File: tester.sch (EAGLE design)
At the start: 74 parts, among them IC1 ATmega8/88/168, K1 NA 05W K, M1 SP6000C-180, P1 250, P2 10k lin, Q1 BC847CSMD, Q2 BC847CSMD, Q3 BC328-40, Q4 8,000 MHz, Q5 BC847CSMD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

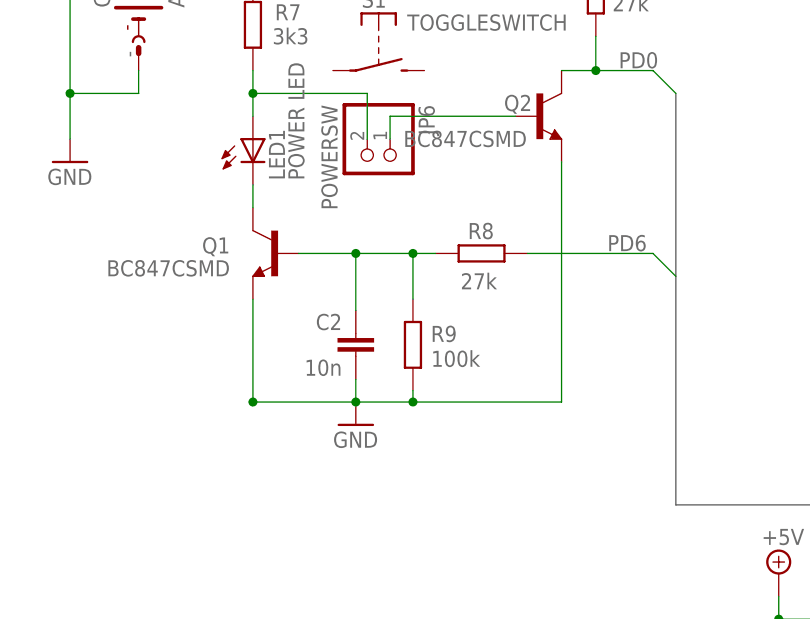
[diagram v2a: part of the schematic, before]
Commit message: rearranged some parts, variant without pwm
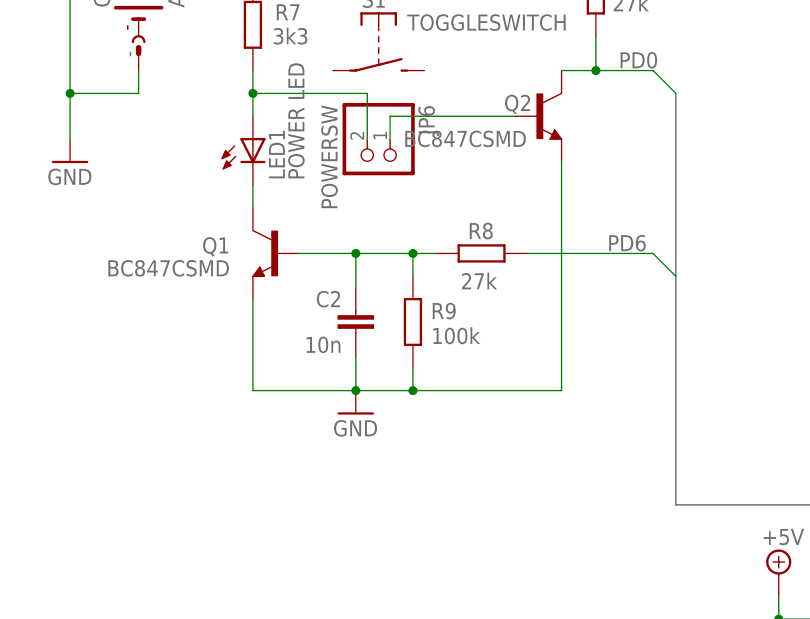
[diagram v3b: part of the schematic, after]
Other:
- moved on the sheet: C2, R9
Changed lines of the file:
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@@
 </attributes>
 <variantdefs>
+<variantdef name="nopwm"/>
 </variantdefs>
 <classes>
@@
 <part name="G1" library="battery" deviceset="AB9V" device=""/>
 <part name="JP2" library="con-lsta" deviceset="FE05-1" device="" value="TEST"/>
-<part name="U4" library="linear" deviceset="LM339" device="D" value="LM339D"/>
-<part name="P2" library="pot" deviceset="TRIM_EU-" device="CA9V" value="10k lin"/>
-<part name="R19" library="resistor" deviceset="R-EU_" device="R0603" value="10k"/>
-<part name="C9" library="resistor" deviceset="C-EU" device="C0603" value="100n"/>
-<part name="R20" library="resistor" deviceset="R-EU_" device="R0603" value="100k"/>
-<part name="R21" library="resistor" deviceset="R-EU_" device="R0603" value="10k"/>
-<part name="R22" library="resistor" deviceset="R-EU_" device="R0603" value="12k"/>
-<part name="R23" library="resistor" deviceset="R-EU_" device="R0603" value="10k"/>
-<part name="C10" library="resistor" deviceset="C-EU" device="C0603" value="100n"/>
+<part name="U4" library="linear" deviceset="LM339" device="D" value="LM339D">
+<variant name="nopwm" populate="no"/>
+</part>
+<part name="P2" library="pot" deviceset="TRIM_EU-" device="CA9V" value="10k lin">
+<variant name="nopwm" populate="no"/>
+</part>
+<part name="R19" library="resistor" deviceset="R-EU_" device="R0603" value="10k">
+<variant name="nopwm" populate="no"/>
+</part>
+<part name="C9" library="resistor" deviceset="C-EU" device="C0603" value="100n">
+<variant name="nopwm" populate="no"/>
+</part>
+<part name="R20" library="resistor" deviceset="R-EU_" device="R0603" value="100k">
+<variant name="nopwm" populate="no"/>
+</part>
+<part name="R21" library="resistor" deviceset="R-EU_" device="R0603" value="10k">
+<variant name="nopwm" populate="no"/>
+</part>
+<part name="R22" library="resistor" deviceset="R-EU_" device="R0603" value="12k">
+<variant name="nopwm" populate="no"/>
+</part>
+<part name="R23" library="resistor" deviceset="R-EU_" device="R0603" value="10k">
+<variant name="nopwm" populate="no"/>
+</part>
+<part name="C10" library="resistor" deviceset="C-EU" device="C0603" value="100n">
+<variant name="nopwm" populate="no"/>
+</part>
 <part name="R24" library="resistor" deviceset="R-EU_" device="R0603" value="3k3"/>
 <part name="GND5" library="supply1" deviceset="GND" device=""/>
@@
 <attribute name="VALUE" x="89.1032" y="155.2702" size="1.778" layer="96" rot="MR180"/>
 </instance>
-<instance part="R9" gate="G$1" x="83.82" y="147.32" smashed="yes" rot="MR90">
-<attribute name="NAME" x="85.8012" y="149.4282" size="1.778" layer="95" rot="MR180"/>
-<attribute name="VALUE" x="85.8266" y="146.6596" size="1.778" layer="96" rot="MR180"/>
-</instance>
-<instance part="C2" gate="G$1" x="77.47" y="148.59" smashed="yes" rot="MR0">
-<attribute name="NAME" x="75.946" y="148.971" size="1.778" layer="95" rot="MR0"/>
-<attribute name="VALUE" x="75.946" y="143.891" size="1.778" layer="96" rot="MR0"/>
+<instance part="R9" gate="G$1" x="83.82" y="149.86" smashed="yes" rot="MR90">
+<attribute name="NAME" x="85.8012" y="151.9682" size="1.778" layer="95" rot="MR180"/>
+<attribute name="VALUE" x="85.8266" y="149.1996" size="1.778" layer="96" rot="MR180"/>
+</instance>
+<instance part="C2" gate="G$1" x="77.47" y="151.13" smashed="yes" rot="MR0">
+<attribute name="NAME" x="75.946" y="151.511" size="1.778" layer="95" rot="MR0"/>
+<attribute name="VALUE" x="75.946" y="146.431" size="1.778" layer="96" rot="MR0"/>
 </instance>
 <instance part="R1" gate="G$1" x="248.92" y="193.04" smashed="yes" rot="R90">
@@
 <instance part="P+1" gate="+5V" x="177.8" y="223.52"/>
 <instance part="P+5" gate="+5V" x="66.04" y="252.73"/>
-<instance part="GND9" gate="1" x="77.47" y="138.43"/>
+<instance part="GND9" gate="1" x="77.47" y="139.7"/>
 <instance part="SUPPLY4" gate="1" x="83.82" y="212.09"/>
 <instance part="P+7" gate="+5V" x="163.83" y="175.26" smashed="yes">
@@
 <segment>
 <pinref part="Q1" gate="G$1" pin="E"/>
-<wire x1="66.04" y1="152.4" x2="66.04" y2="140.97" width="0.1524" layer="91"/>
-<junction x="66.04" y="140.97"/>
+<wire x1="66.04" y1="152.4" x2="66.04" y2="142.24" width="0.1524" layer="91"/>
 <pinref part="C2" gate="G$1" pin="2"/>
-<wire x1="77.47" y1="140.97" x2="77.47" y2="143.51" width="0.1524" layer="91"/>
+<wire x1="77.47" y1="142.24" x2="77.47" y2="146.05" width="0.1524" layer="91"/>
 <pinref part="R9" gate="G$1" pin="1"/>
-<wire x1="83.82" y1="142.24" x2="83.82" y2="140.97" width="0.1524" layer="91"/>
-<wire x1="83.82" y1="140.97" x2="77.47" y2="140.97" width="0.1524" layer="91"/>
-<junction x="77.47" y="140.97"/>
+<wire x1="83.82" y1="144.78" x2="83.82" y2="142.24" width="0.1524" layer="91"/>
+<wire x1="83.82" y1="142.24" x2="77.47" y2="142.24" width="0.1524" layer="91"/>
+<junction x="77.47" y="142.24"/>
 <pinref part="GND9" gate="1" pin="GND"/>
-<wire x1="77.47" y1="140.97" x2="66.04" y2="140.97" width="0.1524" layer="91"/>
+<wire x1="77.47" y1="142.24" x2="66.04" y2="142.24" width="0.1524" layer="91"/>
 <pinref part="Q2" gate="G$1" pin="E"/>
-<wire x1="100.33" y1="140.97" x2="100.33" y2="167.64" width="0.1524" layer="91"/>
-<wire x1="83.82" y1="140.97" x2="100.33" y2="140.97" width="0.1524" layer="91"/>
-<junction x="83.82" y="140.97"/>
+<wire x1="100.33" y1="142.24" x2="100.33" y2="167.64" width="0.1524" layer="91"/>
+<wire x1="83.82" y1="142.24" x2="100.33" y2="142.24" width="0.1524" layer="91"/>
+<junction x="83.82" y="142.24"/>
 </segment>
 <segment>
@@
 <wire x1="71.12" y1="157.48" x2="77.47" y2="157.48" width="0.1524" layer="91"/>
 <pinref part="C2" gate="G$1" pin="1"/>
-<wire x1="77.47" y1="157.48" x2="77.47" y2="151.13" width="0.1524" layer="91"/>
+<wire x1="77.47" y1="157.48" x2="77.47" y2="153.67" width="0.1524" layer="91"/>
 <wire x1="77.47" y1="157.48" x2="83.82" y2="157.48" width="0.1524" layer="91"/>
 <pinref part="R9" gate="G$1" pin="2"/>
-<wire x1="83.82" y1="157.48" x2="83.82" y2="152.4" width="0.1524" layer="91"/>
+<wire x1="83.82" y1="157.48" x2="83.82" y2="154.94" width="0.1524" layer="91"/>
 <junction x="77.47" y="157.48"/>
 <pinref part="R8" gate="G$1" pin="2"/>

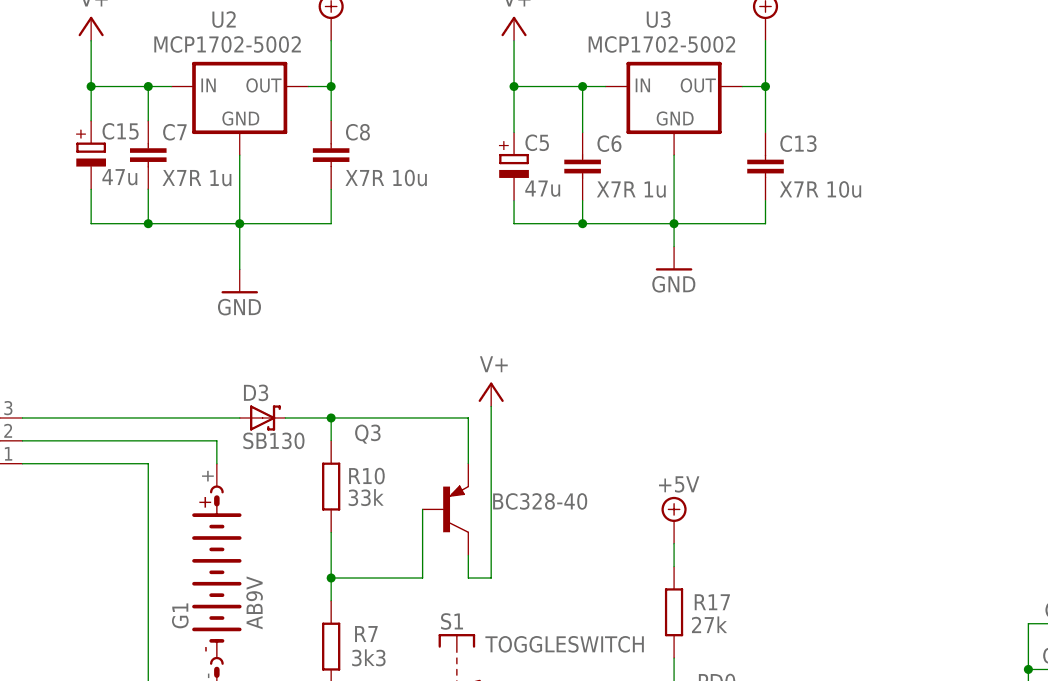
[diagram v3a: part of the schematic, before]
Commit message: smd for q3
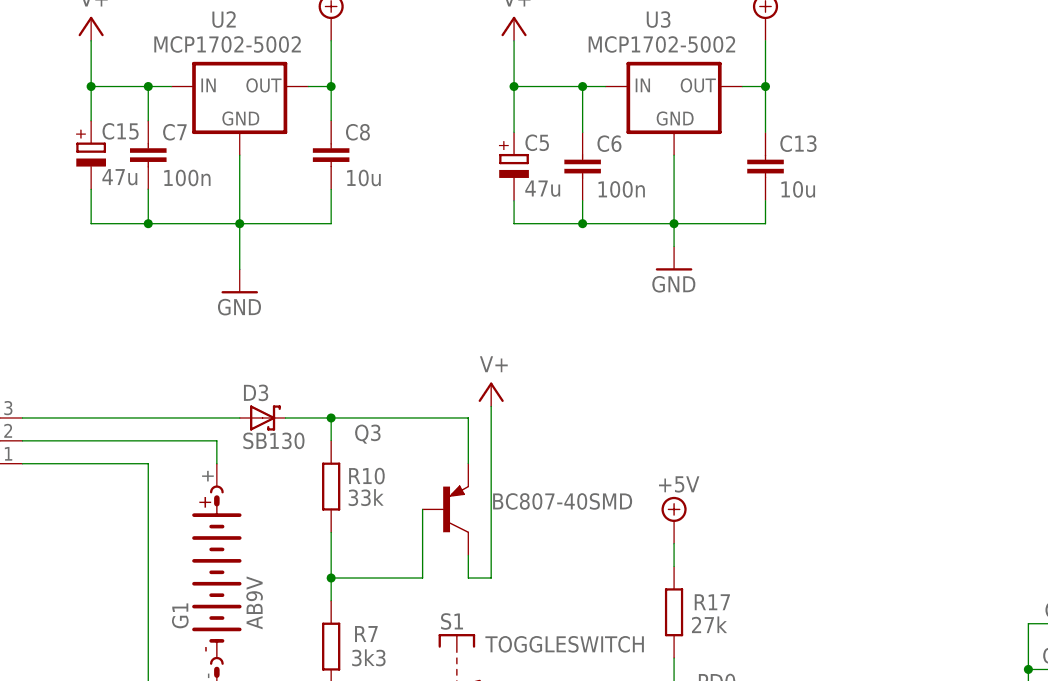
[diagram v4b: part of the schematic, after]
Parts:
- C13, C8: value X7R 10u -> 10u
- C6, C7: value X7R 1u -> 100n
- Q3: value BC328-40 -> BC807-40SMD; device transistor-pnp:BC328-40 -> transistor-pnp:BC807-40SMD
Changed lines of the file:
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@@
 <part name="C4" library="resistor" deviceset="C-EU" device="C0603" value="100n"/>
 <part name="FRAME1" library="markus" deviceset="FRAME_A3" device="" value="frame"/>
-<part name="Q3" library="transistor-pnp" deviceset="BC328*" device="" technology="-40"/>
+<part name="Q3" library="transistor-pnp" deviceset="BC807*" device="SMD" technology="-40"/>
 <part name="D3" library="markus" deviceset="SCHOTTKY-DIODE" device="_RAD3-5-A" value="SB130"/>
 <part name="LED1" library="led" deviceset="LED" device="5MMEXT" value="POWER LED"/>
@@
 <part name="GND6" library="supply1" deviceset="GND" device=""/>
 <part name="Q9" library="transistor-power" deviceset="IRF?5305" device="R" value="IRFR9024"/>
-<part name="C6" library="rcl" deviceset="C-EU" device="C0603" value="X7R 1u"/>
-<part name="C13" library="rcl" deviceset="C-EU" device="C0603" value="X7R 10u"/>
+<part name="C6" library="rcl" deviceset="C-EU" device="C0603" value="100n"/>
+<part name="C13" library="rcl" deviceset="C-EU" device="C0603" value="10u"/>
 <part name="C14" library="rcl" deviceset="C-EU" device="C0603" value="1u"/>
 <part name="DC1" library="dc-dc-converter" deviceset="NMA" device="" value="5V/+-15V"/>
@@
 <part name="SUPPLY9" library="supply2" deviceset="V+" device=""/>
 <part name="SUPPLY10" library="supply2" deviceset="V+" device=""/>
-<part name="C7" library="rcl" deviceset="C-EU" device="C0603" value="X7R 1u"/>
-<part name="C8" library="rcl" deviceset="C-EU" device="C0603" value="X7R 10u"/>
+<part name="C7" library="rcl" deviceset="C-EU" device="C0603" value="100n"/>
+<part name="C8" library="rcl" deviceset="C-EU" device="C0603" value="10u"/>
 <part name="C15" library="rcl" deviceset="CPOL-EU" device="UD-5X5,8" value="47u"/>
 <part name="P1" library="pot" deviceset="TRIM_EU-" device="CA6H" value="250"/>
